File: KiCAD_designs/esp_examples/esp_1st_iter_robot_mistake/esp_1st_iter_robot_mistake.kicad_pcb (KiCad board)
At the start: 2 copper layers, 57 x 37 mm, 22 parts, among them J1 B2B-PH-SM4-TBLFSN, J2 B2B-PH-SM4-TBLFSN, J3 Conn_01x02_Pin, J4 B2B-PH-SM4-TBLFSN, J5 Conn_01x02_Pin, SW2 RS-282G05A3-SM RT, SW3 RS-282G05A3-SM RT, U1 ESP-12F, U2 AMS1117-3.3, U3 CPT-9019S-SMT-TR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

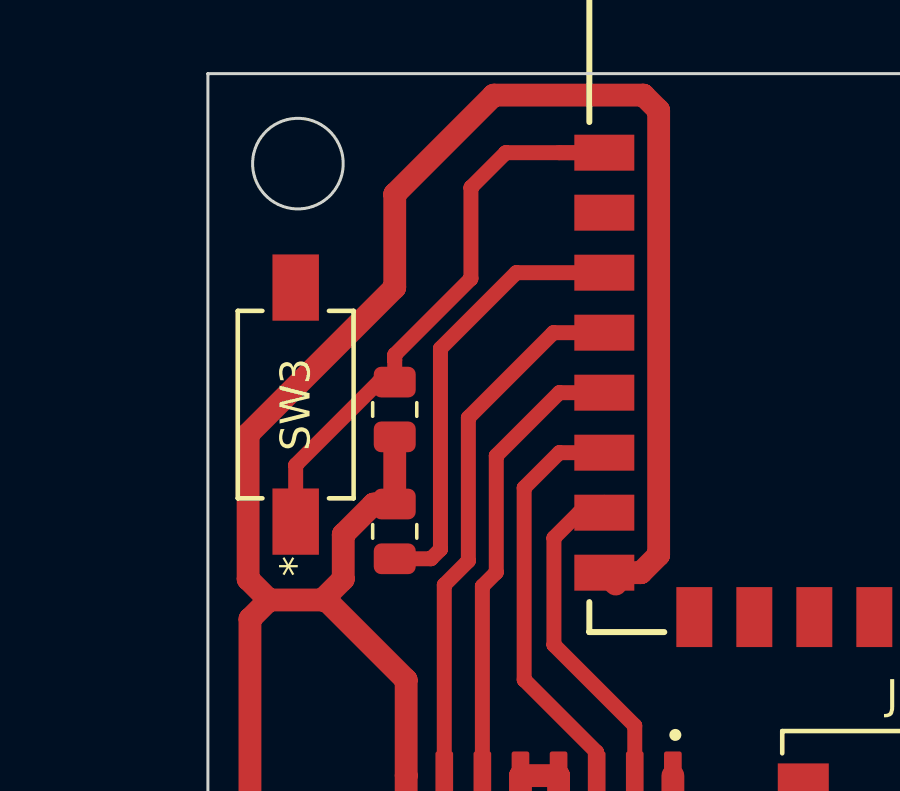
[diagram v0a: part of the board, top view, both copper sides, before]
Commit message: cam_roller_redesign
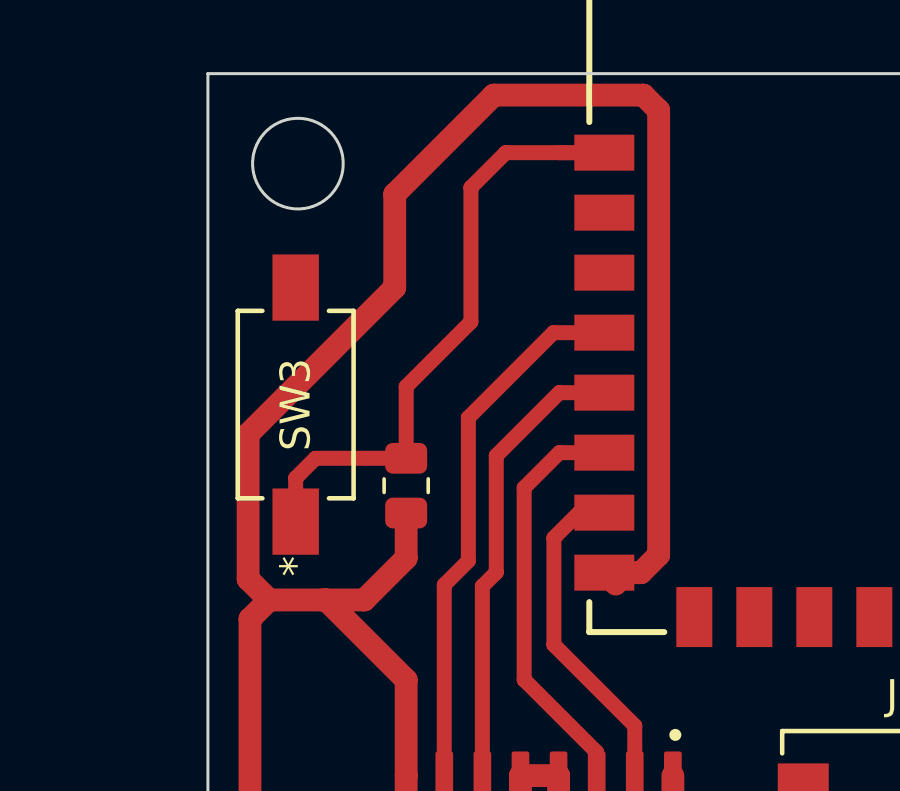
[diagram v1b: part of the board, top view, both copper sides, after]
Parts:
- removed R4: R, Resistor_SMD:R_0805_2012Metric
- moved R1 2.57 mm to (46.6, 38.7)
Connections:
- U1 pad 3: Net-(U1-EN) -> unconnected-(U1-EN-Pad3)
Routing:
- net Net-(U1-EN): track 14.9 -> 0.00 mm
- net VCC: track 195.0 -> 192.7 mm
- net Net-(U1-RST): track 18.8 -> 20.3 mm
